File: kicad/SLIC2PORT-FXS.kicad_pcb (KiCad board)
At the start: 2 copper layers, 100 x 80 mm, 110 parts, among them J1 USB-C_PWR, J2 DC5V_IN, J5 EXPANSION, J6 UART_DBG, J7 SEL_Z_JMP, Q1 AO3401A, Q2 2N7002, SW1 RST, SW2 BOOT, U1 M5StampS3/S3A, U2 74HCT244, U3 CD4053B, U48 P3100SC, U49 1N4004, U50 1N4004, U51 1N4004, U52 1N4004, U53 BZT03C82, U57 BLM21_600R, U72 1N4004, U75 P3100SC, U76 1N4004, U77 1N4004, U78 1N4004, U79 1N4004, U80 BZT03C82, U84 BLM21_600R, U99 1N4004

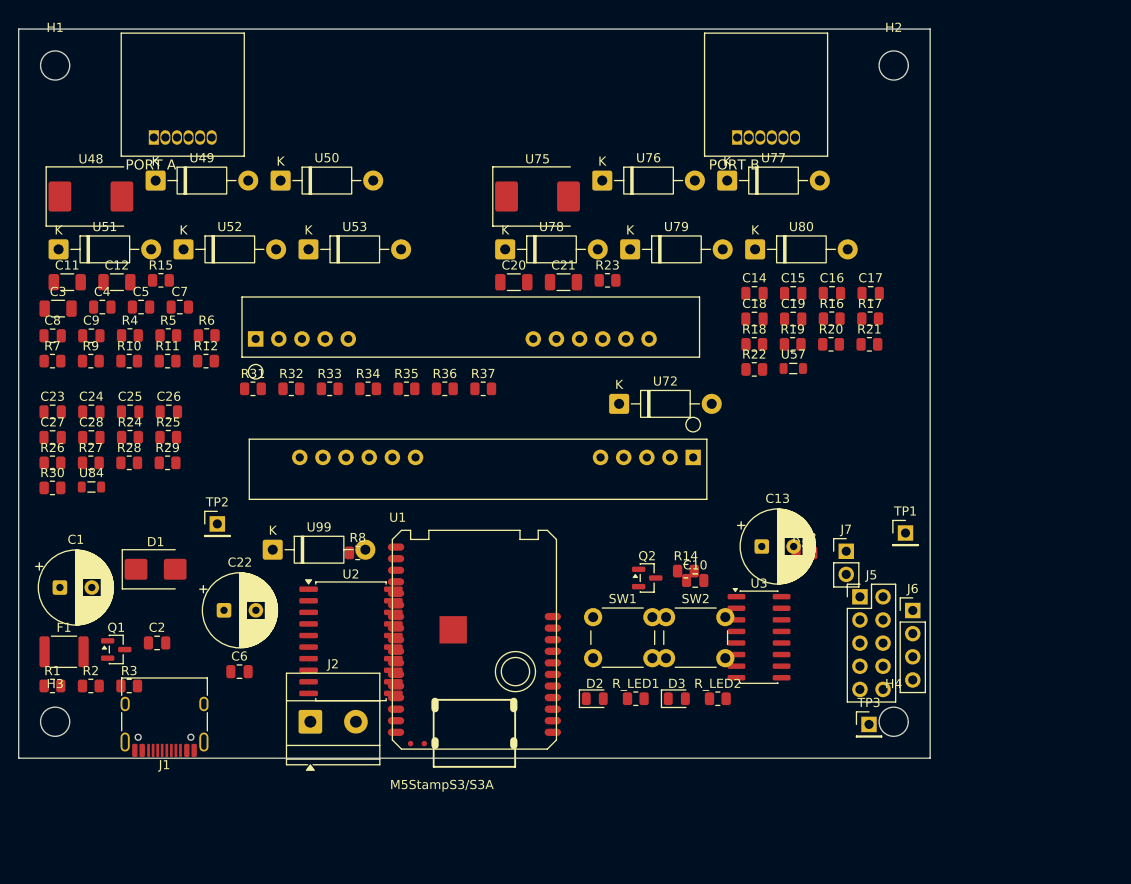
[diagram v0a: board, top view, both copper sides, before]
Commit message: Add placed (unrouted) PCB v3: relay design, 34 TPs, U1 socket, 120x90mm
Regenerated from the current netlist (142 parts). G5V-2 relays placed
next to the audio area with drivers/flyback diodes adjacent, all 34
test points placed near their signals with net-name silk labels, U1 on
the new Stamp-S3-Socket footprint with its courtyard kept empty.
Verified by kicad/check_v3.py: pad-net mismatches NONE, courtyard
overlaps 2 pairs (both inherited from v2; zero new pairs, down from
17 in v2 / 38 in the first 120x80 attempt). Routing is done in EasyEDA.
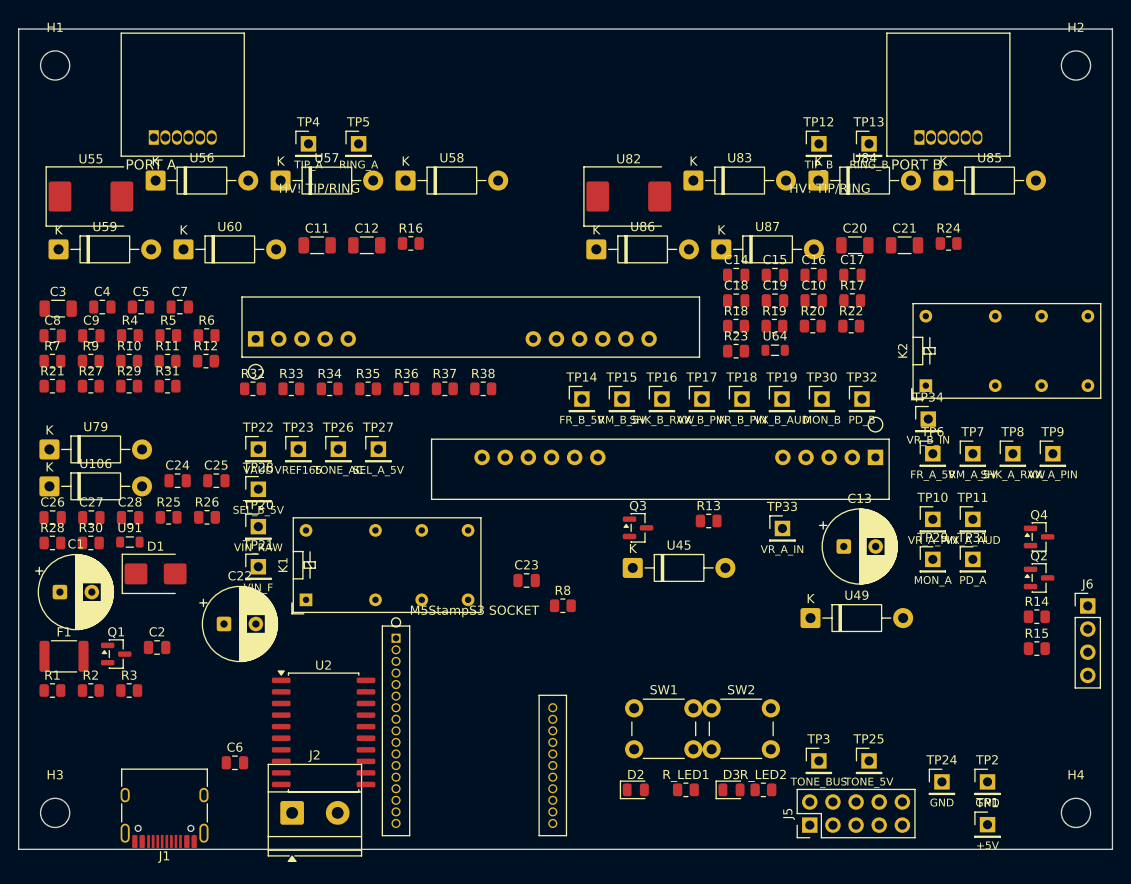
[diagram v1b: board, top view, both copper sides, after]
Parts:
- removed J7: SEL_Z_JMP, PinHeader_1x02_P2.54mm_Vertical
- removed U3: CD4053B, SOIC-16_3.9x9.9mm_P1.27mm
- removed U48, U75: P3100SC, D_SMC
- removed U50, U51, U52, U72, U76, U77, U78, U99: 1N4004, D_DO-41_SOD81_P10.16mm_Horizontal
- removed U53, U80: BZT03C82, D_DO-41_SOD81_P10.16mm_Horizontal
- added K1: G5V-2_DC5, Relay_DPDT_Omron_G5V-2, F.Cu at (31.5, 62.6)
- added K2: G5V-2_DC5, Relay_DPDT_Omron_G5V-2, F.Cu at (99.5, 39.1)
- added Q3: 2N7002, SOT-23, F.Cu at (68.0, 54.7)
- added Q4: 2N7002, SOT-23, F.Cu at (112.0, 55.7)
- added R38: 100K, R_0805_2012Metric, F.Cu at (51.0, 39.5)
- added TP10: VR_A_PIN, PinHeader_1x01_P2.54mm_Vertical, F.Cu at (100.3, 53.8)
- added TP11: VX_A_AUD, PinHeader_1x01_P2.54mm_Vertical, F.Cu at (104.7, 53.8)
- added TP12: TIP_B, PinHeader_1x01_P2.54mm_Vertical, F.Cu at (87.8, 12.6)
- added TP13: RING_B, PinHeader_1x01_P2.54mm_Vertical, F.Cu at (93.3, 12.6)
- added TP14: FR_B_5V, PinHeader_1x01_P2.54mm_Vertical, F.Cu at (61.8, 40.6)
- added TP15: RM_B_5V, PinHeader_1x01_P2.54mm_Vertical, F.Cu at (66.2, 40.6)
- added TP16: SHK_B_RAW, PinHeader_1x01_P2.54mm_Vertical, F.Cu at (70.6, 40.6)
- added TP17: VX_B_PIN, PinHeader_1x01_P2.54mm_Vertical, F.Cu at (75.0, 40.6)
- added TP18: VR_B_PIN, PinHeader_1x01_P2.54mm_Vertical, F.Cu at (79.4, 40.6)
- added TP19: VX_B_AUD, PinHeader_1x01_P2.54mm_Vertical, F.Cu at (83.7, 40.6)
- added TP20: VIN_RAW, PinHeader_1x01_P2.54mm_Vertical, F.Cu at (26.3, 54.6)
- added TP21: VIN_F, PinHeader_1x01_P2.54mm_Vertical, F.Cu at (26.3, 59.0)
- added TP22: VAUD, PinHeader_1x01_P2.54mm_Vertical, F.Cu at (26.3, 46.1)
- added TP23: VREF165, PinHeader_1x01_P2.54mm_Vertical, F.Cu at (30.7, 46.1)
- added TP24: GND, PinHeader_1x01_P2.54mm_Vertical, F.Cu at (101.3, 82.6)
- added TP25: TONE_5V, PinHeader_1x01_P2.54mm_Vertical, F.Cu at (93.3, 80.3)
- added TP26: TONE_AC, PinHeader_1x01_P2.54mm_Vertical, F.Cu at (35.1, 46.1)
- added TP27: SEL_A_5V, PinHeader_1x01_P2.54mm_Vertical, F.Cu at (39.5, 46.1)
- added TP28: SEL_B_5V, PinHeader_1x01_P2.54mm_Vertical, F.Cu at (26.3, 50.5)
- added TP29: MON_A, PinHeader_1x01_P2.54mm_Vertical, F.Cu at (100.3, 58.2)
- added TP30: MON_B, PinHeader_1x01_P2.54mm_Vertical, F.Cu at (88.1, 40.6)
- added TP31: PD_A, PinHeader_1x01_P2.54mm_Vertical, F.Cu at (104.7, 58.2)
- added TP32: PD_B, PinHeader_1x01_P2.54mm_Vertical, F.Cu at (92.5, 40.6)
- added TP33: VR_A_IN, PinHeader_1x01_P2.54mm_Vertical, F.Cu at (83.8, 54.8)
- added TP34: VR_B_IN, PinHeader_1x01_P2.54mm_Vertical, F.Cu at (99.8, 42.8)
- added TP4: TIP_A, PinHeader_1x01_P2.54mm_Vertical, F.Cu at (31.8, 12.6)
- added TP5: RING_A, PinHeader_1x01_P2.54mm_Vertical, F.Cu at (37.3, 12.6)
- added TP6: FR_A_5V, PinHeader_1x01_P2.54mm_Vertical, F.Cu at (100.3, 46.6)
- added TP7: RM_A_5V, PinHeader_1x01_P2.54mm_Vertical, F.Cu at (104.7, 46.6)
- added TP8: SHK_A_RAW, PinHeader_1x01_P2.54mm_Vertical, F.Cu at (109.1, 46.6)
- added TP9: VX_A_PIN, PinHeader_1x01_P2.54mm_Vertical, F.Cu at (113.5, 46.6)
- added U106: 1N4007, D_DO-41_SOD81_P10.16mm_Horizontal, F.Cu at (3.38, 50.2)
- added U45: 1N4007, D_DO-41_SOD81_P10.16mm_Horizontal, F.Cu at (67.4, 59.1)
- added U55: P3100SC, D_SMC, F.Cu at (7.92, 18.4)
- added U56: 1N4007, D_DO-41_SOD81_P10.16mm_Horizontal, F.Cu at (15.0, 16.6)
- added U58: 1N4007, D_DO-41_SOD81_P10.16mm_Horizontal, F.Cu at (42.4, 16.6)
- added U59: 1N4007, D_DO-41_SOD81_P10.16mm_Horizontal, F.Cu at (4.38, 24.2)
- added U60: BZT03C82, D_DO-41_SOD81_P10.16mm_Horizontal, F.Cu at (18.1, 24.2)
- added U64: BK2125HS601-T, L_0805_2012Metric, F.Cu at (83.0, 35.2)
- added U82: P3100SC, D_SMC, F.Cu at (66.9, 18.4)
- added U83: 1N4007, D_DO-41_SOD81_P10.16mm_Horizontal, F.Cu at (74.0, 16.6)
- added U85: 1N4007, D_DO-41_SOD81_P10.16mm_Horizontal, F.Cu at (101.4, 16.6)
- added U86: 1N4007, D_DO-41_SOD81_P10.16mm_Horizontal, F.Cu at (63.4, 24.2)
- added U87: BZT03C82, D_DO-41_SOD81_P10.16mm_Horizontal, F.Cu at (77.1, 24.2)
- added U91: BK2125HS601-T, L_0805_2012Metric, F.Cu at (12.2, 56.3)
- R13, R21, R29: value 10K -> 100K
- R15, R23: value 27K -> 100K
- R16, R24: value 10K -> 27K
- R17, R25: value 18K -> 10K
- R18, R26: value 100K -> 18K
- R19, R27: value 0R -> 100K
- R20, R28: value 100K -> 0R
- R22, R30: value 100K -> 10K
- TP1: value TP -> +5V
- TP2: value TP -> GND
- TP3: value TP -> TONE_BUS
- U1: footprint Stamp-S3-SMD -> Stamp-S3-Socket
- U49, U79: value 1N4004 -> 1N4007
- U57, U84: value BLM21_600R -> 1N4007; footprint L_0805_2012Metric -> D_DO-41_SOD81_P10.16mm_Horizontal
- moved R15 104.2 mm to (111.7, 68.0)
- moved R24 92.3 mm to (102.0, 23.5)
- moved R21 89.7 mm to (3.71, 39.2)
- moved TP2 89.1 mm to (106.3, 82.6)
- moved U84 86.5 mm to (87.7, 16.6)
- moved U49 86.4 mm to (86.9, 64.6)
- moved U79 67.4 mm to (3.38, 46.1)
- moved U57 59.9 mm to (28.7, 16.6)
- moved C23 55.2 mm to (55.7, 60.5)
- moved R16 46.9 mm to (43.0, 23.5)
- moved Q2 43.0 mm to (112.0, 60.2)
- moved R14 38.8 mm to (111.7, 64.5)
- moved C20 37.6 mm to (91.7, 23.7)
- moved C21 37.6 mm to (97.2, 23.7)
- moved C10 33.3 mm to (87.2, 29.8)
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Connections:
- R13 pad 1: SEL_Z -> SEL_A_5V
- R14 pad 1: PD_EN -> SEL_B_5V
- R15 pad 1: TIP_A -> PD_EN
- R15 pad 2: RING_A -> GND
- R16 pad 1: SHK_A_RAW -> TIP_A
- R16 pad 2: SHK_A_33 -> RING_A
- R17 pad 1: SHK_A_33 -> SHK_A_RAW
- R17 pad 2: GND -> SHK_A_33
- R18 pad 1: VX_A_AUD -> SHK_A_33
- R18 pad 2: VAUD -> GND
- R19 pad 2: VX_A_IN -> VAUD
- R20 pad 1: TAP_A_N -> VX_A_AUD
- R20 pad 2: VREF165 -> VX_A_IN
- R21 pad 2: MON_A -> VREF165
- R22 pad 1: VR_A_IN -> TAP_A_N
- R22 pad 2: VAUD -> MON_A
- R23 pad 1: TIP_B -> VR_A_IN
- R23 pad 2: RING_B -> VAUD
- R24 pad 1: SHK_B_RAW -> TIP_B
- R24 pad 2: SHK_B_33 -> RING_B
- R25 pad 1: SHK_B_33 -> SHK_B_RAW
- R25 pad 2: GND -> SHK_B_33
- R26 pad 1: VX_B_AUD -> SHK_B_33
- R26 pad 2: VAUD -> GND
- R27 pad 2: VX_B_IN -> VAUD
- R28 pad 1: TAP_B_N -> VX_B_AUD
- R28 pad 2: VREF165 -> VX_B_IN
- R29 pad 2: MON_B -> VREF165
- R30 pad 1: VR_B_IN -> TAP_B_N
- R30 pad 2: VAUD -> MON_B
- R31 pad 1: FR_A_33 -> VR_B_IN
- R31 pad 2: GND -> VAUD
- R32 pad 1: RM_A_33 -> FR_A_33
- R33 pad 1: SEL_A_33 -> RM_A_33
- R34 pad 1: TONE_PWM_33 -> SEL_A_33
- R35 pad 1: FR_B_33 -> TONE_PWM_33
- R36 pad 1: RM_B_33 -> FR_B_33
- R37 pad 1: SEL_B_33 -> RM_B_33
- TP3 pad 1: AUX_TP -> TONE_BUS
- U49 pad 1: BRP_A -> +5V
- U49 pad 2: TIP_A -> RLY_B_COIL
- U57 pad 1: +5V -> BRP_A
- U57 pad 2: +5V_PA -> RING_A
- U79 pad 1: RING_B -> PD_BUS
- U79 pad 2: BRM_B -> PD_A
- U84 pad 1: +5V -> BRP_B
- U84 pad 2: +5V_PB -> RING_B
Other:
- board size 100 x 80 mm -> 120 x 90 mm
- board text added: "HV! TIP/RING"
- board text added: "M5StampS3 SOCKET"

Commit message: Round 5 (v3.1): move decoupling caps next to their loads
- C6 beside U2 (74HCT244) pin 20 VCC: centre-to-pad 17.0 -> 4.4mm
- C23 (+5V_PB) above MOD_B pin 10: 13.7 -> 4.7mm
- C14 (+5V_PA) under MOD_A pin 10: 14.0 -> 3.7mm
- C10 (+5V) flipped to B.Cu under U1 socket pin 13: 69.5 -> 1.9mm
  (top side is hemmed in by U2/J2/board edge; single bottom part)
- Bulk swap: C13 (+5V_PA) to port-A side next to K1, C22 (+5V_PB)
  under MOD_B: 35.9 -> 10.0mm from MOD_B pin 10
- C3/C4/C5 verified clustered with VAUD/VREF dividers (4.7-10.4mm)
- check_v31: pad-net mismatches NONE, layer-aware courtyard pairs
  identical to v3 (2 inherited pairs, no new), no other part moved
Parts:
- C10: moved to B.Cu
- moved C13 68.5 mm to (22.5, 65.3)
- moved C10 68.3 mm to (43.3, 82.1)
- moved C22 32.7 mm to (54.1, 57.0)
- moved C23 18.4 mm to (53.2, 42.3)
- moved C14 16.6 mm to (66.0, 37.7)
- moved C6 15.8 mm to (34.5, 69.0)

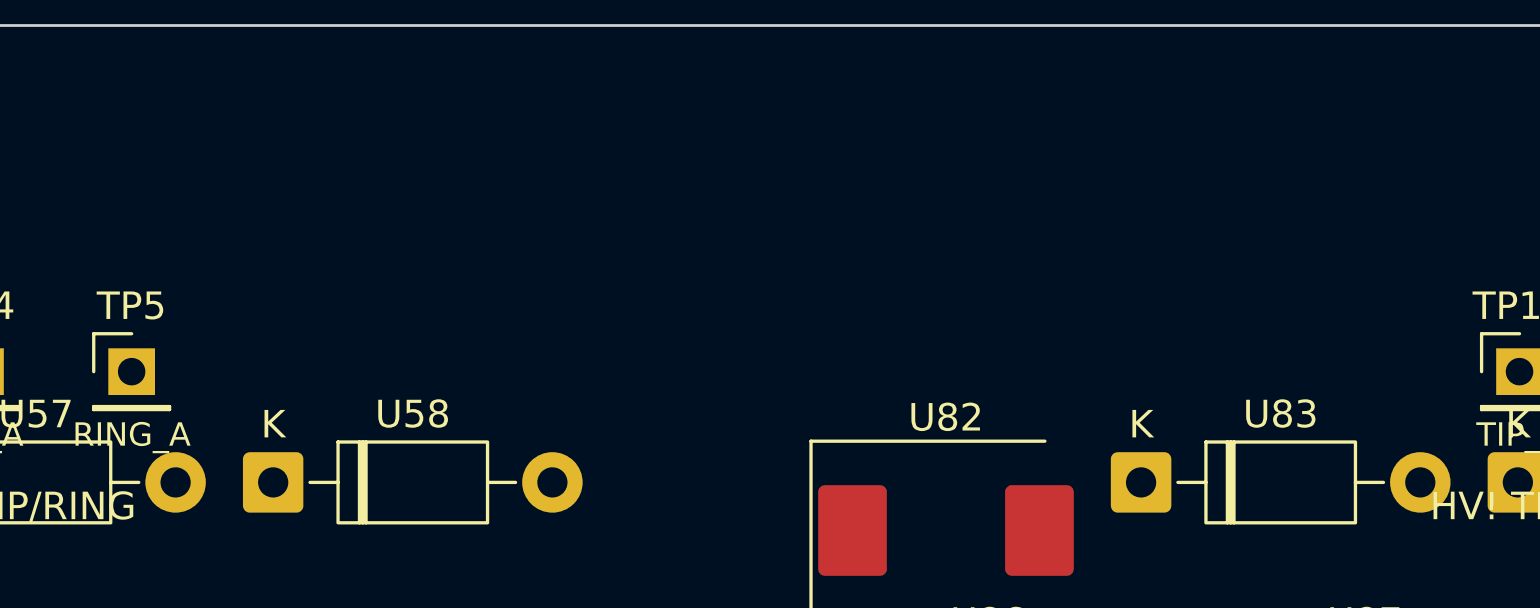
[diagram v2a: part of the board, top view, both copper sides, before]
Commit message: Board v3.2: place status LEDs on the top-edge strip (156 parts)
All 142 v3.1 placements keep their exact coordinates. The 14 new
parts (D4-D9, R_LED3-R_LED8, Q5/Q6) go into the freescan-verified
empty strip along the top edge, grouped per port next to its RJ11:
row 1 = HOOK and RING resistor/LED pairs, row 2 = HOOK buffer FET
and LINK pair, with HOOK_x / RING_x / LINK_x role silk labels.
check_v32: 160 footprints (156 + 4 MH), pad-net mismatches NONE,
courtyard overlap pairs unchanged vs v3.1 (2 inherited pairs,
zero new), C10 still the only B.Cu part, TP labels intact.
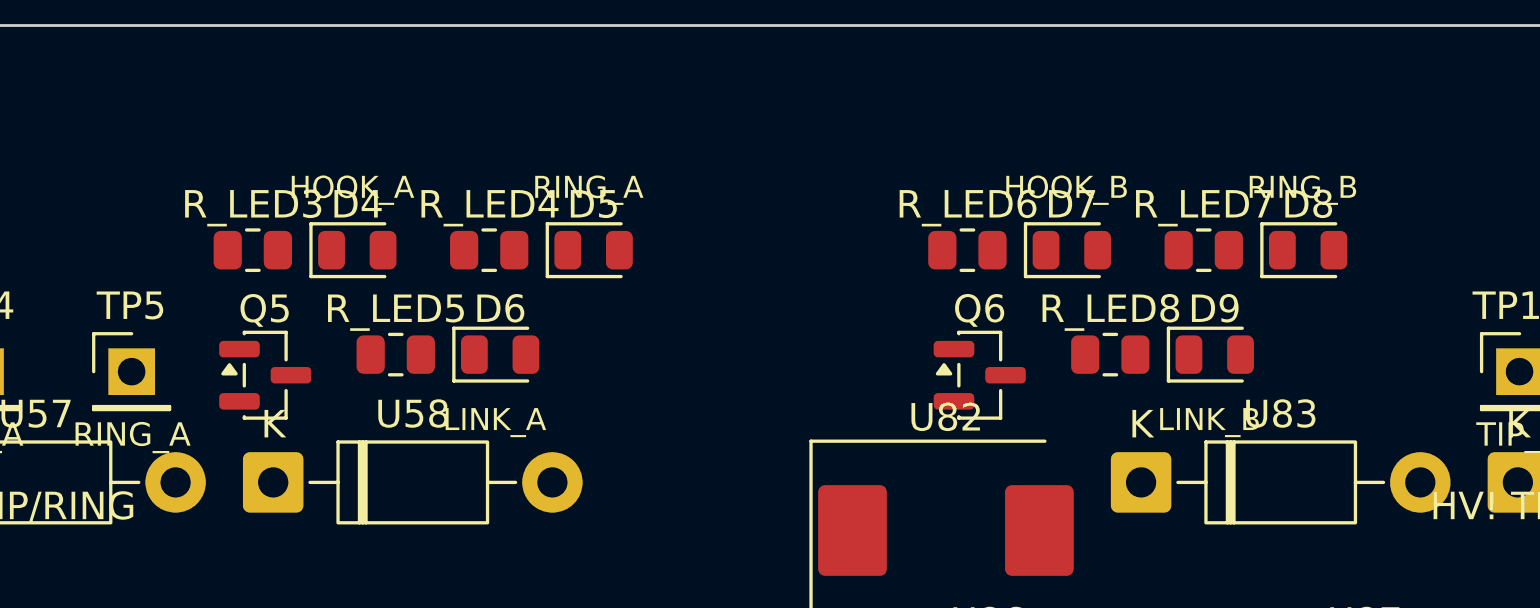
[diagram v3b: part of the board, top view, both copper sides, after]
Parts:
- added D4: LED_GRN, LED_0805_2012Metric, F.Cu at (45.5, 8.18)
- added D5: LED_YEL, LED_0805_2012Metric, F.Cu at (54.1, 8.18)
- added D6: LED_BLU, LED_0805_2012Metric, F.Cu at (50.7, 12.0)
- added D7: LED_GRN, LED_0805_2012Metric, F.Cu at (71.5, 8.18)
- added D8: LED_YEL, LED_0805_2012Metric, F.Cu at (80.1, 8.18)
- added D9: LED_BLU, LED_0805_2012Metric, F.Cu at (76.7, 12.0)
- added Q5: 2N7002, SOT-23, F.Cu at (42.2, 12.7)
- added Q6: 2N7002, SOT-23, F.Cu at (68.2, 12.7)
- added R_LED3: 1.5K, R_0805_2012Metric, F.Cu at (41.7, 8.18)
- added R_LED4: 1.5K, R_0805_2012Metric, F.Cu at (50.3, 8.18)
- added R_LED5: 1K, R_0805_2012Metric, F.Cu at (46.9, 12.0)
- added R_LED6: 1.5K, R_0805_2012Metric, F.Cu at (67.7, 8.18)
- added R_LED7: 1.5K, R_0805_2012Metric, F.Cu at (76.3, 8.18)
- added R_LED8: 1K, R_0805_2012Metric, F.Cu at (72.9, 12.0)
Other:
- board text added: "HOOK_A"
- board text added: "HOOK_B"
- board text added: "LINK_A"
- board text added: "LINK_B"
- board text added: "RING_A"
- board text added: "RING_B"

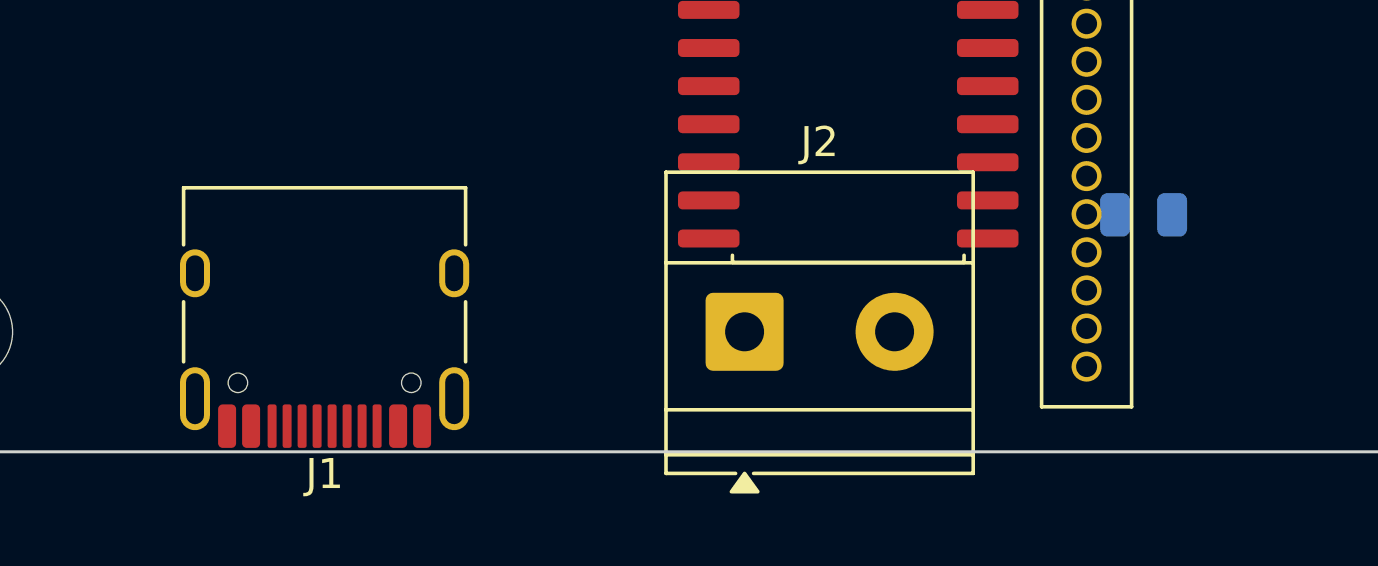
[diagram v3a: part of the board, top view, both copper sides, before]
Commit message: Board v3.3: standard numbered net format so EasyEDA imports nets
KiCad 10 pcbnew serializes pad nets name-only ((net "NAME"), no net
table); EasyEDA KiCad importer drops them (Nets=None, 0 ratsnest).
fix_net_format.py rewrites to classic numbered form: board-level
(net N "NAME") declarations + numbered pad nets. Verified by pcbnew
reload: 84 nets + net 0, pad assignments identical to netlist_v32.json.

Also two DRC adjudications from the EasyEDA report:
- J1 (USB-C): nudged 0.2 mm inward; pad-to-edge 0.13 -> 0.33 mm
  (EasyEDA rule 0.3 mm). Footprint is an edge-placement design
  (courtyard overhangs the edge by design); shell face now 1.45 mm
  inside the edge, no mating impact.
- C10 (back-side 100nF under U1 socket): overlapped U1.13 annular
  ring by 50 um (same net) and sat 191 um from U1.14. Shifted
  +0.35 mm in x; true copper gaps to U1.12/13/14 now 479/300/457 um,
  pad centre to U1.13 centre still 1.30 mm.
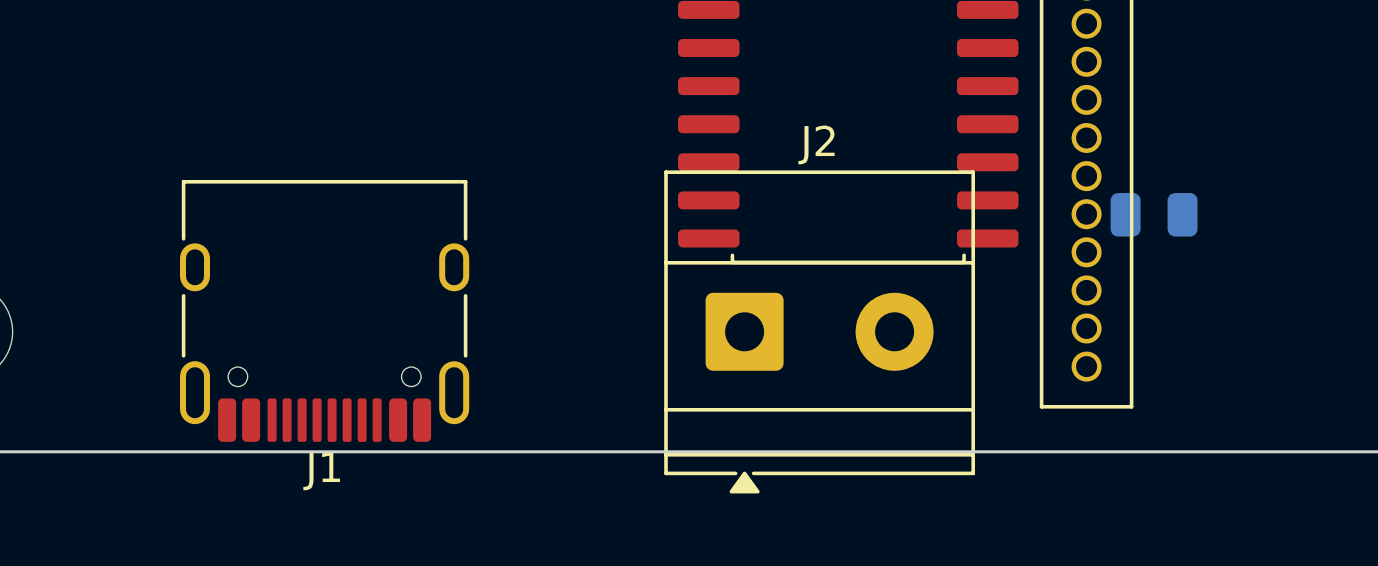
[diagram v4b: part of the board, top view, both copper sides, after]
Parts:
- moved C10 0.35 mm to (43.6, 82.1)
- moved J1 0.20 mm to (16.0, 84.9)
